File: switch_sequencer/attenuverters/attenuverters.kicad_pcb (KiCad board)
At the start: 2 copper layers, 50.6 x 128.5 mm, 68 parts, among them J1 Eurorack_Power_10pin_Shrouded, J10 3.5mm_Mono_Switched_sm, J11 3.5mm_Mono_Switched_sm, J12 3.5mm_Mono_Switched_sm, J13 3.5mm_Mono_Switched_sm, J14 3.5mm_Mono_Switched_sm, J15 3.5mm_Mono_Switched_sm, J16 3.5mm_Mono_Switched_sm, J17 3.5mm_Mono_Switched_sm, J18 Conn_01x03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

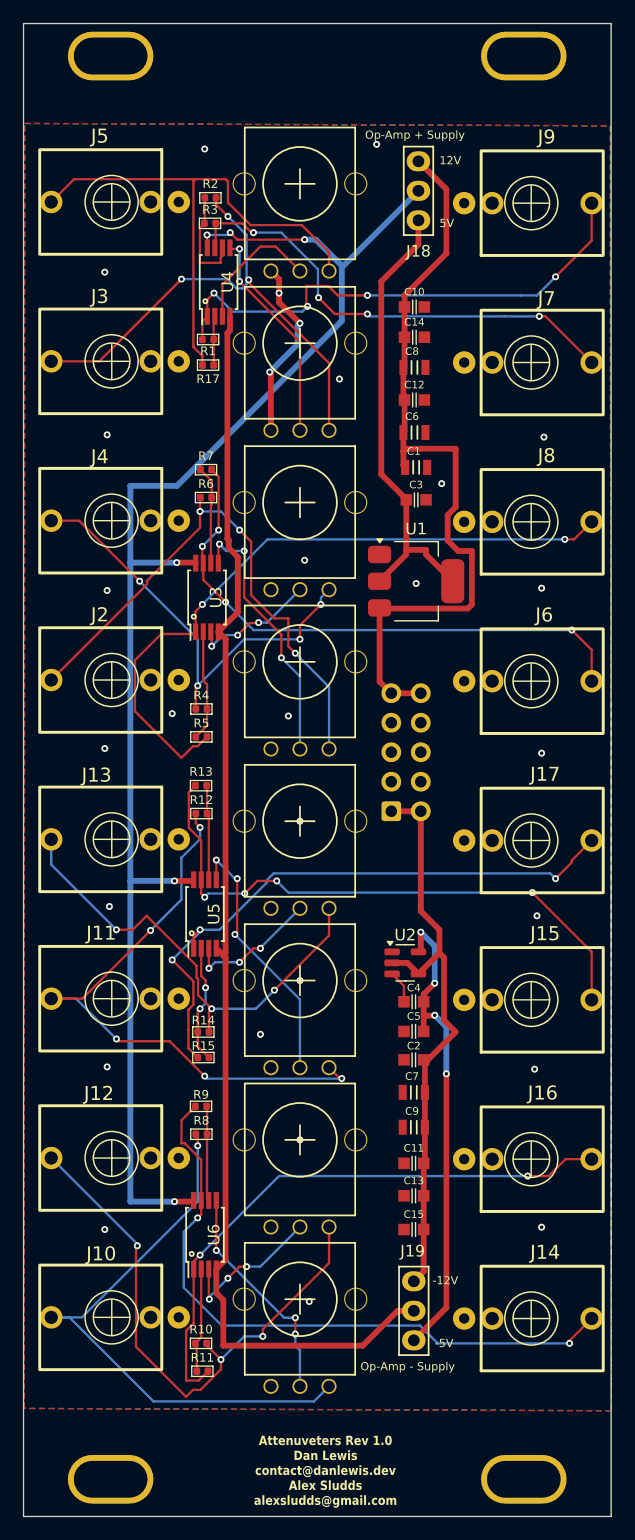
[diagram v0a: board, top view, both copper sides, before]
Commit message: finish attenuverters, sample and hold
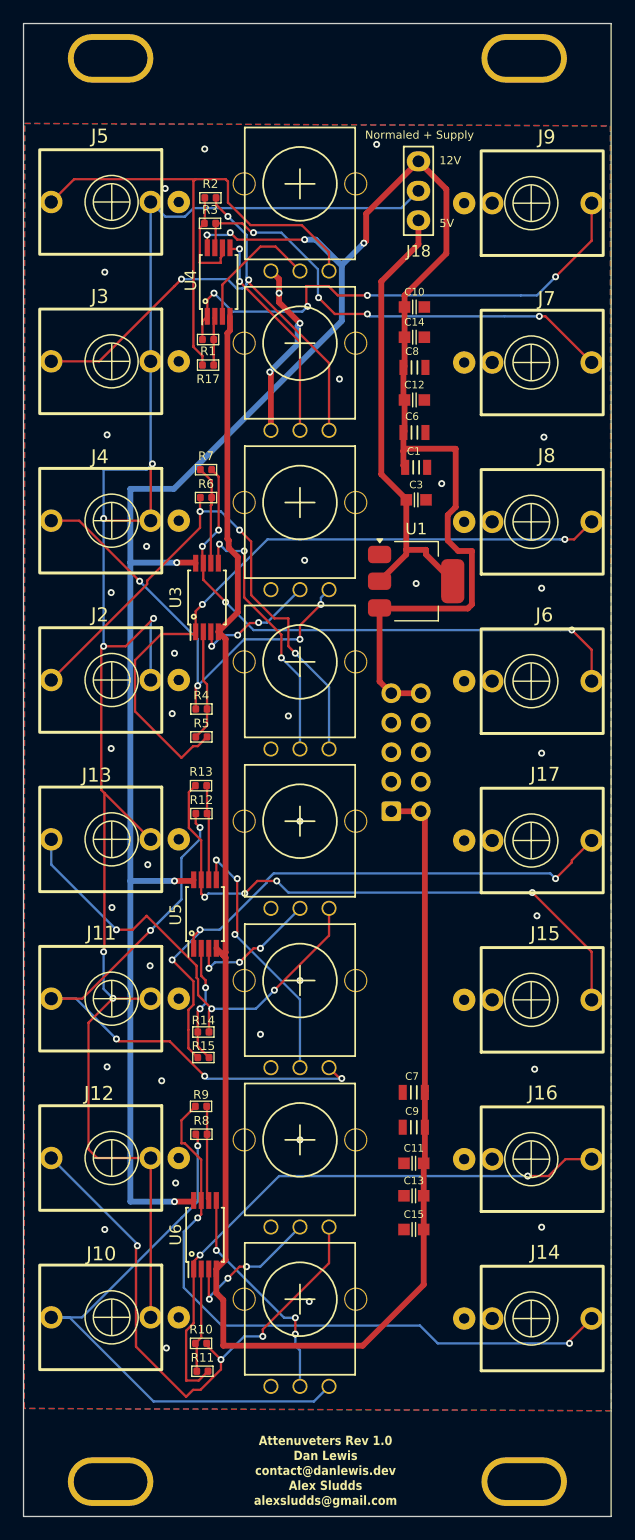
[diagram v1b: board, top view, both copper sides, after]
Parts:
- removed ? (x4): , 
- removed C2: 1uF_0603_25V, 4ms_Capacitor:C_0603
- removed C4: 10nF_0603_25V, 4ms_Capacitor:C_0603
- removed C5: 10uF_0603_10V, 4ms_Capacitor:C_0603
- removed J19: Conn_01x03, 4ms_Connector:Pins_1x03_2.54mm_TH
- removed U2: LT1964-5, Package_TO_SOT_SMD:TSOT-23-5
- added H1: MountingHole, 4ms_Faceplate:Faceplate_Rail_Mount_Slot_Plated, F.Cu at (133.9, 38.8)
- added H2: MountingHole, 4ms_Faceplate:Faceplate_Rail_Mount_Slot_Plated, F.Cu at (169.5, 38.8)
- added H3: MountingHole, 4ms_Faceplate:Faceplate_Rail_Mount_Slot_Plated, F.Cu at (133.9, 161.3)
- added H4: MountingHole, 4ms_Faceplate:Faceplate_Rail_Mount_Slot_Plated, F.Cu at (169.5, 161.3)
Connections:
- J10 pad 3: GNDA -> NORMALED_IN
- J11 pad 3: GNDA -> NORMALED_IN
- J12 pad 3: GNDA -> NORMALED_IN
- J13 pad 3: GNDA -> NORMALED_IN
- J14 pad 3: GNDA -> unconnected-(J14-SW-Pad3)
- J15 pad 3: GNDA -> unconnected-(J15-SW-Pad3)
- J16 pad 3: GNDA -> unconnected-(J16-SW-Pad3)
- J17 pad 3: GNDA -> unconnected-(J17-SW-Pad3)
- J18 pad 2: op_amp_positive_supply -> NORMALED_IN
- J2 pad 3: GNDA -> NORMALED_IN
- J3 pad 3: GNDA -> NORMALED_IN
- J4 pad 3: GNDA -> NORMALED_IN
- J5 pad 3: GNDA -> NORMALED_IN
- J6 pad 3: GNDA -> unconnected-(J6-SW-Pad3)
- J7 pad 3: GNDA -> unconnected-(J7-SW-Pad3)
- J8 pad 3: GNDA -> unconnected-(J8-SW-Pad3)
- J9 pad 3: GNDA -> unconnected-(J9-SW-Pad3)
- U3 pad 4: op_amp_negative_supply -> -12VA
- U3 pad 8: op_amp_positive_supply -> +12V
- U4 pad 4: op_amp_negative_supply -> -12VA
- U4 pad 8: op_amp_positive_supply -> +12V
- U5 pad 4: op_amp_negative_supply -> -12VA
- U5 pad 8: op_amp_positive_supply -> +12V
- U6 pad 4: op_amp_negative_supply -> -12VA
- U6 pad 8: op_amp_positive_supply -> +12V
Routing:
- net NORMALED_IN: track 0.00 -> 159.5 mm, vias 0 -> 6
- net +12V: track 67.3 -> 200.5 mm, vias 0 -> 7
- net op_amp_positive_supply: track 130.4 -> 0.00 mm, vias 6 -> 0
- net op_amp_negative_supply: track 109.2 -> 0.00 mm
- net -12VA: track 51.4 -> 154.6 mm
- net minus_5V: track 41.7 -> 0.00 mm, vias 4 -> 0
- net Net-(U2-BYP): track 2.82 -> 0.00 mm
- net GNDA: vias 29 -> 37
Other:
- board text added: "Normaled + Supply"
- board text removed: "-12V"
- board text removed: "-5V"
- board text removed: "Op-Amp + Supply"
- board text removed: "Op-Amp - Supply"

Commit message: attenuverters
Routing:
- net -12VA: track 154.6 -> 159.7 mm
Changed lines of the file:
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@@
 			(at 0 0)
 			(size 7.366 4.191)
-			(drill oval 6.35 3.175)
+			(drill oval 6.3 3.175)
 			(layers "*.Cu" "*.Mask")
 			(remove_unused_layers no)
@@
 			(at 0 0)
 			(size 7.366 4.191)
-			(drill oval 6.35 3.175)
+			(drill oval 6.3 3.175)
 			(layers "*.Cu" "*.Mask")
 			(remove_unused_layers no)
@@
 			(at 0 0)
 			(size 7.366 4.191)
-			(drill oval 6.35 3.175)
+			(drill oval 6.3 3.175)
 			(layers "*.Cu" "*.Mask")
 			(remove_unused_layers no)
@@
 			(at 0 0)
 			(size 7.366 4.191)
-			(drill oval 6.35 3.175)
+			(drill oval 6.3 3.175)
 			(layers "*.Cu" "*.Mask")
 			(remove_unused_layers no)
@@
 	)
 	(segment
-		(start 149.2 87)
-		(end 148 87)
-		(width 0.2)
-		(layer "F.Cu")
-		(net 1)
-	)
-	(segment
 		(start 141.6 79.2)
 		(end 141.6 77.8)
@@
 	)
 	(segment
-		(start 148 87)
-		(end 146 85)
-		(width 0.2)
-		(layer "F.Cu")
-		(net 1)
-	)
-	(segment
-		(start 141.6 76.63)
-		(end 141.63 76.6)
+		(start 149.2 89.4)
+		(end 149.2 83.4)
 		(width 0.2)
 		(layer "F.Cu")
@@
 	)
 	(segment
-		(start 128.793 92.305355)
-		(end 137.05 84.048355)
+		(start 149.8 90)
+		(end 149.2 89.4)
 		(width 0.2)
 		(layer "F.Cu")
@@
 	)
 	(segment
-		(start 146 80.4)
-		(end 145 79.4)
+		(start 141.6 76.63)
+		(end 141.63 76.6)
 		(width 0.2)
 		(layer "F.Cu")
@@
 	)
 	(segment
-		(start 146 85)
-		(end 146 80.4)
+		(start 128.793 92.305355)
+		(end 137.05 84.048355)
 		(width 0.2)
 		(layer "F.Cu")
@@
 	)
 	(segment
-		(start 149.8 90)
-		(end 149.2 89.4)
-		(width 0.2)
-		(layer "F.Cu")
-		(net 1)
-	)
-	(segment
-		(start 149.2 89.4)
-		(end 149.2 87)
+		(start 149.2 83.4)
+		(end 146.2 80.4)
 		(width 0.2)
 		(layer "F.Cu")
@@
 	)
 	(via
-		(at 145 79.4)
+		(at 146.2 80.4)
 		(size 0.6)
 		(drill 0.3)
@@
 	)
 	(segment
-		(start 145 79.4)
-		(end 143.4 77.8)
+		(start 141.6 77.8)
+		(end 143.8 77.8)
+		(width 0.2)
+		(layer "B.Cu")
+		(net 1)
+	)
+	(segment
+		(start 143.8 77.8)
+		(end 146.2 80.2)
 		(width 0.2)
 		(layer "B.Cu")
@@
 	)
 	(segment
-		(start 143.4 77.8)
-		(end 141.6 77.8)
+		(start 146.2 80.2)
+		(end 146.2 80.4)
 		(width 0.2)
 		(layer "B.Cu")
@@
 	)
 	(segment
-		(start 143.038478 141.4)
-		(end 148.838478 147.2)
+		(start 149.8 149.6)
+		(end 150.2 150)
 		(width 0.2)
 		(layer "B.Cu")
@@
 	)
 	(segment
-		(start 148.838478 147.2)
+		(start 148.969239 147.2)
 		(end 149.8 147.2)
 		(width 0.2)
@@
 	)
 	(segment
-		(start 149.8 149.6)
-		(end 150.2 150)
+		(start 149.8 148.6)
+		(end 149.8 149.6)
 		(width 0.2)
 		(layer "B.Cu")
@@
 	)
 	(segment
-		(start 149.8 148.6)
-		(end 149.8 149.6)
+		(start 143.169239 141.4)
+		(end 148.969239 147.2)
 		(width 0.2)
 		(layer "B.Cu")
@@
 	(segment
 		(start 143 141.4)
-		(end 143.038478 141.4)
+		(end 143.169239 141.4)
 		(width 0.2)
 		(layer "B.Cu")
@@
 	)
 	(segment
-		(start 144.068794 80.275012)
-		(end 143.95 80.156218)
+		(start 143.8 72.7)
+		(end 147 75.9)
 		(width 0.5)
 		(layer "F.Cu")
@@
 	)
 	(segment
-		(start 143.175 88.15)
-		(end 144.85 86.475)
+		(start 143.8 115.1)
+		(end 143.8 88.775)
 		(width 0.5)
 		(layer "F.Cu")
@@
 	)
 	(segment
-		(start 144.175 62.225)
-		(end 144.175 61)
+		(start 143.8 115.75)
+		(end 143.8 115.1)
 		(width 0.5)
 		(layer "F.Cu")
@@
 	)
 	(segment
-		(start 160.85 139.6)
-		(end 160.85 144.35)
+		(start 143.8 62.6)
+		(end 143.8 72.7)
 		(width 0.5)
 		(layer "F.Cu")
@@
 	)
 	(segment
-		(start 144.068794 80.937754)
-		(end 144.068794 80.275012)
+		(start 160.85 139.6)
+		(end 160.85 144.35)
 		(width 0.5)
 		(layer "F.Cu")
@@
 	)
 	(segment
+		(start 144.175 62.225)
+		(end 143.8 62.6)
+		(width 0.5)
+		(layer "F.Cu")
+		(net 18)
+	)
+	(segment
 		(start 160.95 130.8)
 		(end 160.95 133.8)
@@
 	)
 	(segment
+		(start 143.8 115.1)
+		(end 143.8 117.8)
+		(width 0.5)
+		(layer "F.Cu")
+		(net 18)
+	)
+	(segment
 		(start 160.95 127.8)
 		(end 160.95 130.8)
@@
 	)
 	(segment
-		(start 158.06 103.6)
-		(end 160.6 103.6)
+		(start 144.26552 80.256086)
+		(end 144.26552 81.13448)
 		(width 0.5)
 		(layer "F.Cu")
@@
 	)
 	(segment
-		(start 144.85 81.71896)
-		(end 144.068794 80.937754)
+		(start 144.175 61)
+		(end 144.175 62.225)
+		(width 0.5)
+		(layer "F.Cu")
+		(net 18)
+	)
+	(segment
+		(start 158.06 103.6)
+		(end 160.6 103.6)
 		(width 0.5)
 		(layer "F.Cu")
@@
 	)
 	(segment
-		(start 144.85 86.475)
-		(end 144.85 81.71896)
-		(width 0.5)
-		(layer "F.Cu")
-		(net 18)
-	)
-	(segment
-		(start 143.95 62.45)
-		(end 144.175 62.225)
+		(start 147 75.9)
+		(end 147 77.521606)
 		(width 0.5)
 		(layer "F.Cu")
@@
 	)
 	(segment
-		(start 143.95 80.156218)
-		(end 143.95 62.45)
+		(start 160.85 136.7)
+		(end 160.85 139.6)
 		(width 0.5)
 		(layer "F.Cu")
@@
 	)
 	(segment
-		(start 160.85 136.7)
-		(end 160.85 139.6)
+		(start 161.05 127.7)
+		(end 160.95 127.8)
+		(width 0.5)
+		(layer "F.Cu")
+		(net 18)
+	)
+	(segment
+		(start 144.85 86.475)
+		(end 143.175 88.15)
 		(width 0.5)
 		(layer "F.Cu")
@@
 	(segment
 		(start 143.8 142.2)
-		(end 143.8 116.2)
+		(end 143.8 117.8)
 		(width 0.5)
 		(layer "F.Cu")
@@
 	)
 	(segment
-		(start 161.05 127.7)
-		(end 160.95 127.8)
+		(start 144.85 81.71896)
+		(end 144.85 86.475)
 		(width 0.5)
 		(layer "F.Cu")
@@
 	)
 	(segment
-		(start 143.8 115.75)
-		(end 143.8 88.775)
+		(start 147 77.521606)
+		(end 144.26552 80.256086)
+		(width 0.5)
+		(layer "F.Cu")
+		(net 18)
+	)
+	(segment
+		(start 144.26552 81.13448)
+		(end 144.85 81.71896)
+		(width 0.5)
+		(layer "F.Cu")
+		(net 18)
+	)
+	(segment
+		(start 143.8 117.8)
+		(end 143.8 116.2)
 		(width 0.5)
 		(layer "F.Cu")
